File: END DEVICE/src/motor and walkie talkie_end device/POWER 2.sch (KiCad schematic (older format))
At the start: 31 parts, among them IC4 TPS55340RTER, SW6 SW_SPDT, U7 LM117_TO39, U8 LM741

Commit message: third commit:very minor changes
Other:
- moved on the sheet: C35, C37, C44, C45, C?, U?
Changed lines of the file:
@@
 Text Notes 750  4850 0    50   ~ 10
 5V REGULATOR
-Connection ~ 4100 5350
-Wire Wire Line
-	4100 5350 4100 5200
+Connection ~ 4100 5550
+Wire Wire Line
+	4100 5550 4100 5400
 $Comp
 L power:+5V #PWR0173
 U 1 1 61EC74E6
-P 4100 5200
-F 0 "#PWR0173" H 4100 5050 50  0001 C CNN
-F 1 "+5V" H 4115 5373 50  0000 C CNN
-F 2 "" H 4100 5200 50  0001 C CNN
-F 3 "" H 4100 5200 50  0001 C CNN
-	1    4100 5200
-	1    0    0    -1
-$EndComp
-Wire Wire Line
-	1700 5350 1350 5350
-Connection ~ 1700 5350
-Wire Wire Line
-	1700 5500 1700 5350
-Wire Wire Line
-	1100 5500 1100 5350
-Wire Wire Line
-	1450 5700 1700 5700
-Connection ~ 1450 5700
-Wire Wire Line
-	1450 5700 1100 5700
-Wire Wire Line
-	1450 5900 1450 5700
+P 4100 5400
+F 0 "#PWR0173" H 4100 5250 50  0001 C CNN
+F 1 "+5V" H 4115 5573 50  0000 C CNN
+F 2 "" H 4100 5400 50  0001 C CNN
+F 3 "" H 4100 5400 50  0001 C CNN
+	1    4100 5400
+	1    0    0    -1
+$EndComp
+Wire Wire Line
+	1700 5550 1350 5550
+Connection ~ 1700 5550
+Wire Wire Line
+	1700 5700 1700 5550
+Wire Wire Line
+	1100 5700 1100 5550
+Wire Wire Line
+	1450 5900 1700 5900
+Connection ~ 1450 5900
+Wire Wire Line
+	1450 5900 1100 5900
+Wire Wire Line
+	1450 6100 1450 5900
 $Comp
 L power:GND #PWR0174
 U 1 1 61EAEFFC
-P 1450 5900
-F 0 "#PWR0174" H 1450 5650 50  0001 C CNN
-F 1 "GND" H 1455 5727 50  0000 C CNN
-F 2 "" H 1450 5900 50  0001 C CNN
-F 3 "" H 1450 5900 50  0001 C CNN
-	1    1450 5900
-	1    0    0    -1
-$EndComp
-Connection ~ 3750 5700
-Wire Wire Line
-	3750 5900 3750 5700
+P 1450 6100
+F 0 "#PWR0174" H 1450 5850 50  0001 C CNN
+F 1 "GND" H 1455 5927 50  0000 C CNN
+F 2 "" H 1450 6100 50  0001 C CNN
+F 3 "" H 1450 6100 50  0001 C CNN
+	1    1450 6100
+	1    0    0    -1
+$EndComp
+Connection ~ 3750 5900
+Wire Wire Line
+	3750 6100 3750 5900
 $Comp
 L power:GND #PWR0175
 U 1 1 61EA92A1
-P 3750 5900
-F 0 "#PWR0175" H 3750 5650 50  0001 C CNN
-F 1 "GND" H 3755 5727 50  0000 C CNN
-F 2 "" H 3750 5900 50  0001 C CNN
-F 3 "" H 3750 5900 50  0001 C CNN
-	1    3750 5900
+P 3750 6100
+F 0 "#PWR0175" H 3750 5850 50  0001 C CNN
+F 1 "GND" H 3755 5927 50  0000 C CNN
+F 2 "" H 3750 6100 50  0001 C CNN
+F 3 "" H 3750 6100 50  0001 C CNN
+	1    3750 6100
 	1    0    0    -1
 $EndComp
@@
 L power:GND #PWR0176
 U 1 1 61EA7291
-P 2700 5850
-F 0 "#PWR0176" H 2700 5600 50  0001 C CNN
-F 1 "GND" H 2705 5677 50  0000 C CNN
-F 2 "" H 2700 5850 50  0001 C CNN
-F 3 "" H 2700 5850 50  0001 C CNN
-	1    2700 5850
-	1    0    0    -1
-$EndComp
-Wire Wire Line
-	4100 5350 4100 5450
-Wire Wire Line
-	3750 5350 3750 5400
+P 2700 6050
+F 0 "#PWR0176" H 2700 5800 50  0001 C CNN
+F 1 "GND" H 2705 5877 50  0000 C CNN
+F 2 "" H 2700 6050 50  0001 C CNN
+F 3 "" H 2700 6050 50  0001 C CNN
+	1    2700 6050
+	1    0    0    -1
+$EndComp
+Wire Wire Line
+	4100 5550 4100 5650
+Wire Wire Line
+	3750 5550 3750 5600
 $Comp
 L Device:CP1_Small C45
 U 1 1 61E99AAF
-P 3100 5500
-F 0 "C45" H 3191 5546 50  0000 L CNN
-F 1 "2.2uF" H 3191 5455 50  0000 L CNN
-F 2 "" H 3100 5500 50  0001 C CNN
-F 3 "~" H 3100 5500 50  0001 C CNN
-	1    3100 5500
+P 3100 5700
+F 0 "C45" H 3191 5746 50  0000 L CNN
+F 1 "2.2uF" H 3191 5655 50  0000 L CNN
+F 2 "" H 3100 5700 50  0001 C CNN
+F 3 "~" H 3100 5700 50  0001 C CNN
+	1    3100 5700
 	1    0    0    -1
 $EndComp
@@
 L Device:C_Small C37
 U 1 1 61E9952A
-P 1700 5600
-F 0 "C37" H 1792 5646 50  0000 L CNN
-F 1 "1uF" H 1792 5555 50  0000 L CNN
-F 2 "" H 1700 5600 50  0001 C CNN
-F 3 "~" H 1700 5600 50  0001 C CNN
-	1    1700 5600
+P 1700 5800
+F 0 "C37" H 1792 5846 50  0000 L CNN
+F 1 "1uF" H 1792 5755 50  0000 L CNN
+F 2 "" H 1700 5800 50  0001 C CNN
+F 3 "~" H 1700 5800 50  0001 C CNN
+	1    1700 5800
 	1    0    0    -1
 $EndComp
@@
 L Device:CP1_Small C35
 U 1 1 61E98783
-P 1100 5600
-F 0 "C35" H 1191 5646 50  0000 L CNN
-F 1 "10uF" H 1191 5555 50  0000 L CNN
-F 2 "" H 1100 5600 50  0001 C CNN
-F 3 "~" H 1100 5600 50  0001 C CNN
-	1    1100 5600
+P 1100 5800
+F 0 "C35" H 1191 5846 50  0000 L CNN
+F 1 "10uF" H 1191 5755 50  0000 L CNN
+F 2 "" H 1100 5800 50  0001 C CNN
+F 3 "~" H 1100 5800 50  0001 C CNN
+	1    1100 5800
 	1    0    0    -1
 $EndComp
@@
 Wire Wire Line
 	1700 950  1700 1100
-Text GLabel 1100 5200 1    50   Input ~ 0
+Text GLabel 1100 5400 1    50   Input ~ 0
 BATT_IN
 Wire Wire Line
-	1100 5200 1100 5350
-Connection ~ 1100 5350
+	1100 5400 1100 5550
+Connection ~ 1100 5550
 Text GLabel 1800 950  1    50   Input ~ 0
 BATT_IN
@@
 L remote_devices:L4931ABDT50 U?
 U 1 1 62291361
-P 2700 5350
-F 0 "U?" H 2700 5683 50  0000 C CNN
-F 1 "L4931ABDT50" H 2700 5592 50  0000 C CNN
-F 2 "Package_TO_SOT_SMD:TO-252-3_TabPin2" H 2700 5501 50  0000 C CIN
-F 3 "" H 2700 5300 50  0001 C CNN
-	1    2700 5350
-	1    0    0    -1
-$EndComp
-Wire Wire Line
-	1700 5350 2400 5350
-Wire Wire Line
-	3000 5350 3100 5350
-Wire Wire Line
-	2700 5650 2700 5850
-Text GLabel 1350 5200 1    50   Input ~ 10
+P 2700 5550
+F 0 "U?" H 2700 5800 50  0000 C CNN
+F 1 "L4931ABDT50" H 2650 5700 50  0000 C CNN
+F 2 "Package_TO_SOT_SMD:TO-252-3_TabPin2" H 2700 5701 50  0001 C CIN
+F 3 "" H 2700 5500 50  0001 C CNN
+	1    2700 5550
+	1    0    0    -1
+$EndComp
+Wire Wire Line
+	1700 5550 2400 5550
+Wire Wire Line
+	3000 5550 3100 5550
+Wire Wire Line
+	2700 5850 2700 6050
+Text GLabel 1350 5400 1    50   Input ~ 10
 TO_SYS
 Wire Wire Line
-	1350 5200 1350 5350
-Connection ~ 1350 5350
-Wire Wire Line
-	1350 5350 1100 5350
+	1350 5400 1350 5550
+Connection ~ 1350 5550
+Wire Wire Line
+	1350 5550 1100 5550
 Text Notes 3250 6650 0    50   Italic 0
 Regulator can handle up to 20V input \nfrom TO_SYS & BATT_IN
 Wire Wire Line
-	3100 5400 3100 5350
-Connection ~ 3100 5350
-Wire Wire Line
-	3100 5600 3100 5700
+	3100 5600 3100 5550
+Connection ~ 3100 5550
+Wire Wire Line
+	3100 5800 3100 5900
 $Comp
 L Device:CP1_Small C?
 U 1 1 622D1115
-P 4100 5550
-F 0 "C?" H 4191 5596 50  0000 L CNN
-F 1 "10uF" H 4191 5505 50  0000 L CNN
-F 2 "" H 4100 5550 50  0001 C CNN
-F 3 "~" H 4100 5550 50  0001 C CNN
-	1    4100 5550
-	1    0    0    -1
-$EndComp
-Wire Wire Line
-	4100 5700 4100 5650
-Wire Wire Line
-	3750 5700 4100 5700
+P 4100 5750
+F 0 "C?" H 4191 5796 50  0000 L CNN
+F 1 "10uF" H 4191 5705 50  0000 L CNN
+F 2 "" H 4100 5750 50  0001 C CNN
+F 3 "~" H 4100 5750 50  0001 C CNN
+	1    4100 5750
+	1    0    0    -1
+$EndComp
+Wire Wire Line
+	4100 5900 4100 5850
+Wire Wire Line
+	3750 5900 4100 5900
 $Comp
 L Device:C_Small C44
 U 1 1 61E99AB9
-P 3750 5500
-F 0 "C44" H 3842 5546 50  0000 L CNN
-F 1 "1uF" H 3842 5455 50  0000 L CNN
-F 2 "" H 3750 5500 50  0001 C CNN
-F 3 "~" H 3750 5500 50  0001 C CNN
-	1    3750 5500
-	1    0    0    -1
-$EndComp
-Wire Wire Line
-	3750 5600 3750 5700
-Connection ~ 3750 5350
-Wire Wire Line
-	3750 5350 4100 5350
-Wire Wire Line
-	3100 5350 3750 5350
-Wire Wire Line
-	3100 5700 3750 5700
+P 3750 5700
+F 0 "C44" H 3842 5746 50  0000 L CNN
+F 1 "1uF" H 3842 5655 50  0000 L CNN
+F 2 "" H 3750 5700 50  0001 C CNN
+F 3 "~" H 3750 5700 50  0001 C CNN
+	1    3750 5700
+	1    0    0    -1
+$EndComp
+Wire Wire Line
+	3750 5800 3750 5900
+Connection ~ 3750 5550
+Wire Wire Line
+	3750 5550 4100 5550
+Wire Wire Line
+	3100 5550 3750 5550
+Wire Wire Line
+	3100 5900 3750 5900
 Text Notes 1350 7250 0    79   ~ 0
 NB// All components can work when power is pluggedin except the\n         DC-Motor. The motor only works when the battery is connected

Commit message: commit 4:minor changes
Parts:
- gave numbers to parts that had none: 2
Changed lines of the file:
@@
 	1    0    0    -1
 $EndComp
-Wire Wire Line
-	9650 1750 9650 1800
 $Comp
 L Device:R_US R44
@@
 ON=BATTERY LOW\n(<10.5V)
 $Comp
-L power:PWR_FLAG #FLG0104
-U 1 1 6221AB86
-P 9600 1800
-F 0 "#FLG0104" H 9600 1875 50  0001 C CNN
-F 1 "PWR_FLAG" V 9600 1927 50  0000 L CNN
-F 2 "" H 9600 1800 50  0001 C CNN
-F 3 "~" H 9600 1800 50  0001 C CNN
-	1    9600 1800
-	0    -1   -1   0
-$EndComp
-Wire Wire Line
-	9600 1800 9650 1800
-Connection ~ 9650 1800
-Wire Wire Line
-	9650 1800 9650 1900
-$Comp
-L remote_devices:L4931ABDT50 U?
+L remote_devices:L4931ABDT50 U9
 U 1 1 62291361
 P 2700 5550
-F 0 "U?" H 2700 5800 50  0000 C CNN
+F 0 "U9" H 2700 5800 50  0000 C CNN
 F 1 "L4931ABDT50" H 2650 5700 50  0000 C CNN
 F 2 "Package_TO_SOT_SMD:TO-252-3_TabPin2" H 2700 5701 50  0001 C CIN
@@
 	3100 5800 3100 5900
 $Comp
-L Device:CP1_Small C?
+L Device:CP1_Small C50
 U 1 1 622D1115
 P 4100 5750
-F 0 "C?" H 4191 5796 50  0000 L CNN
+F 0 "C50" H 4191 5796 50  0000 L CNN
 F 1 "10uF" H 4191 5705 50  0000 L CNN
 F 2 "" H 4100 5750 50  0001 C CNN
@@
 Text Notes 1350 7250 0    79   ~ 0
 NB// All components can work when power is pluggedin except the\n         DC-Motor. The motor only works when the battery is connected
+Wire Wire Line
+	9650 1750 9650 1900
+$Comp
+L power:PWR_FLAG #FLG?
+U 1 1 62357D8E
+P 1700 5300
+AR Path="/615FCEB9/62357D8E" Ref="#FLG?"  Part="1"
+AR Path="/61DF39DA/62357D8E" Ref="#FLG0104"  Part="1"
+F 0 "#FLG0104" H 1700 5375 50  0001 C CNN
+F 1 "PWR_FLAG" H 1700 5473 50  0000 C CNN
+F 2 "" H 1700 5300 50  0001 C CNN
+F 3 "~" H 1700 5300 50  0001 C CNN
+	1    1700 5300
+	1    0    0    -1
+$EndComp
+Wire Wire Line
+	1700 5300 1700 5550
 $EndSCHEMATC

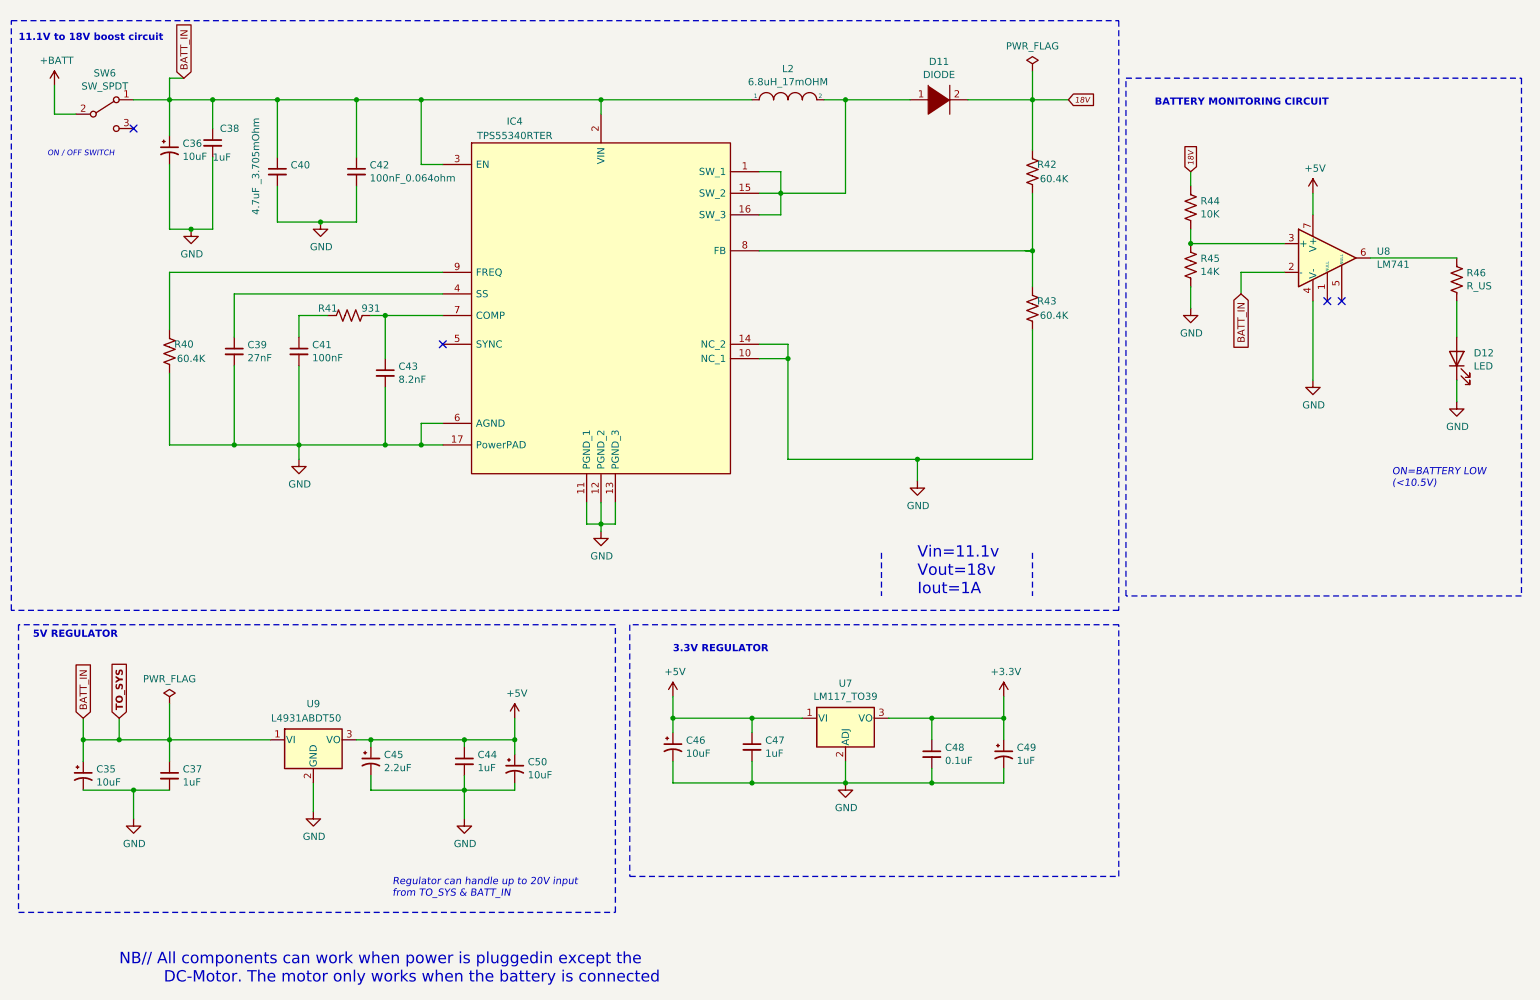
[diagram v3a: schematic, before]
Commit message: All footprint associations updated
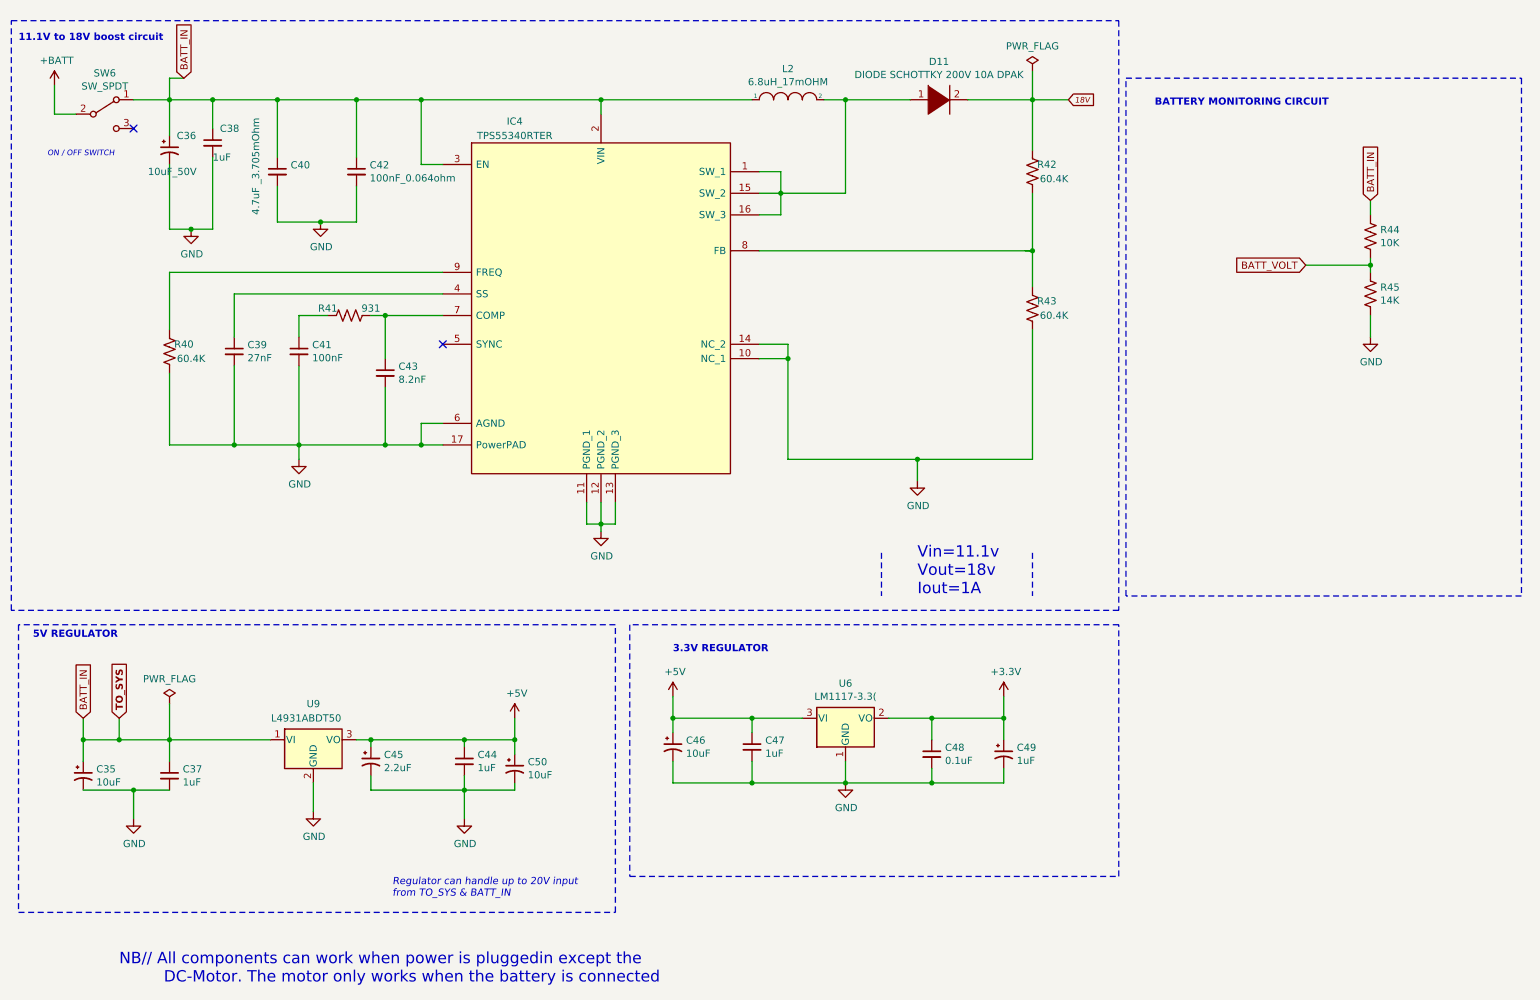
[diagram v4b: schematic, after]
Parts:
- removed D12: LED, symbol Device:LED
- removed R46: R_US, symbol Device:R_US
- removed U7: LM117_TO39, Package_TO_SOT_THT:TO-39-3, symbol Regulator_Linear:LM117_TO39
- removed U8: LM741, symbol Amplifier_Operational:LM741
- added U6: LM1117-3.3(, Package_TO_SOT_SMD:SOT-223, symbol Regulator_Linear:LM1117-3.3
- C35: footprint (none) -> Capacitor_SMD:CP_Elec_4x4.5
- C36: value 10uF -> 10uF_50V; footprint (none) -> Capacitor_Tantalum_SMD:CP_EIA-1608-08_AVX-J
- C37, C38, C39, C40, C41, C42, C43, C44, C47, C48: footprint (none) -> Capacitor_SMD:C_0603_1608Metric
- C45, C46, C49, C50: footprint (none) -> Capacitor_Tantalum_SMD:CP_EIA-2012-12_Kemet-R_Pad1.30x1.05mm_HandSolder
- D11: value DIODE -> DIODE SCHOTTKY 200V 10A DPAK; footprint (none) -> Package_TO_SOT_SMD:TO-252-3_TabPin2
- IC4: footprint QFN50P300X300X80-17N-D -> Package_DFN_QFN:WQFN-16-1EP_3x3mm_P0.5mm_EP1.75x1.75mm_ThermalVias
- L2: footprint (none) -> Remote_devices:SDR1307680KL
- R40, R41, R42, R43, R44, R45: footprint (none) -> Resistor_SMD:R_0603_1608Metric
- SW6: footprint Button_Switch_THT:SW_Slide_1P2T_CK_OS102011MS2Q -> Button_Switch_SMD:SW_SPDT_PCM12
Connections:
- net +3V3: now also U6.2 (VO)
- net +5V: now also U6.3 (VI)
- net 18V: no longer R44.1
- net BATT_IN: now also R44.1
- net GND: now also U6.1 (GND)
- net BATT_VOLT: now reaches R44.2, R45.1
- no-connect marks 4 -> 2
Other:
- note removed: "ON=BATTERY LOW\n(<10.5V)"
- moved on the sheet: R44, R45

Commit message: Project 99% complete and ready:Revision Needed
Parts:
- added C5: 10uF, Capacitor_SMD:C_0603_1608Metric, symbol Device:C_Small
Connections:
- net 18V: now also C5.1
- net GND: now also C5.2
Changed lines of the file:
@@
 Text GLabel 7950 1100 2    39   Input Italic 0
 18V
-Wire Wire Line
-	7950 1100 7700 1100
 Text Notes 650  700  0    50   ~ 10
 11.1V to 18V boost circuit\n
@@
 Wire Notes Line
 	8300 550  8300 4650
-Wire Wire Line
-	7650 2150 7700 2150
 Wire Wire Line
 	5800 2150 7700 2150
@@
 	1    0    0    -1
 $EndComp
+$Comp
+L power:GND #PWR0111
+U 1 1 6290EE9D
+P 8100 1500
+F 0 "#PWR0111" H 8100 1250 50  0001 C CNN
+F 1 "GND" H 8105 1327 50  0000 C CNN
+F 2 "" H 8100 1500 50  0001 C CNN
+F 3 "" H 8100 1500 50  0001 C CNN
+	1    8100 1500
+	1    0    0    -1
+$EndComp
+Wire Wire Line
+	7900 1400 7900 1450
+Wire Wire Line
+	7900 1450 8100 1450
+Wire Wire Line
+	8100 1450 8100 1500
+$Comp
+L Device:C_Small C5
+U 1 1 62905119
+P 7900 1300
+F 0 "C5" H 7992 1346 50  0000 L CNN
+F 1 "10uF" H 7992 1255 50  0000 L CNN
+F 2 "Capacitor_SMD:C_0603_1608Metric" H 7900 1300 50  0001 C CNN
+F 3 "~" H 7900 1300 50  0001 C CNN
+	1    7900 1300
+	1    0    0    -1
+$EndComp
+Wire Wire Line
+	7950 1100 7900 1100
+Wire Wire Line
+	7900 1200 7900 1100
+Connection ~ 7900 1100
+Wire Wire Line
+	7900 1100 7700 1100
 $EndSCHEMATC
